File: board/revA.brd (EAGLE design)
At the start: 50 x 50 mm, 37 parts, among them IC1 74HCT125D, Q1 VND7NV04, Q2 VND7NV04, Q3 VND7NV04, Q4 VND7NV04

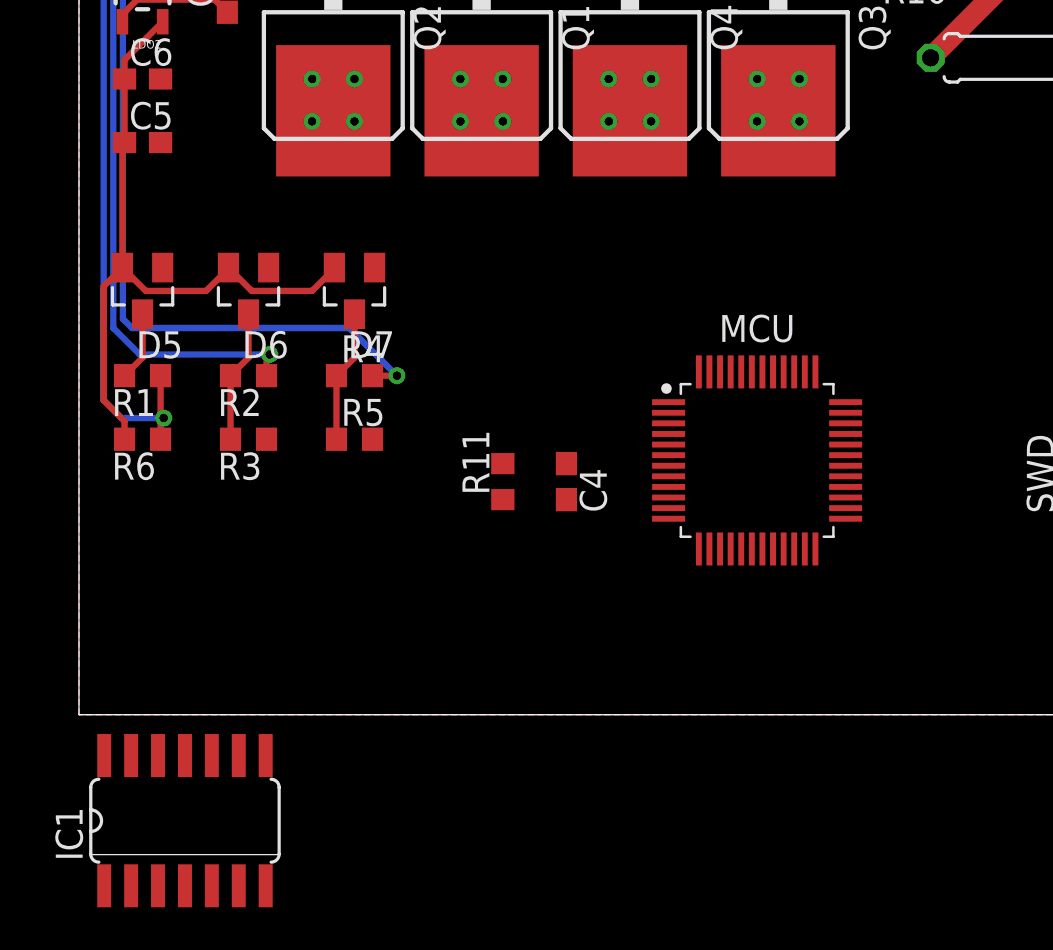
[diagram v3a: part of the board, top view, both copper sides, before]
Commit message: Changing buffer package to TSSOP
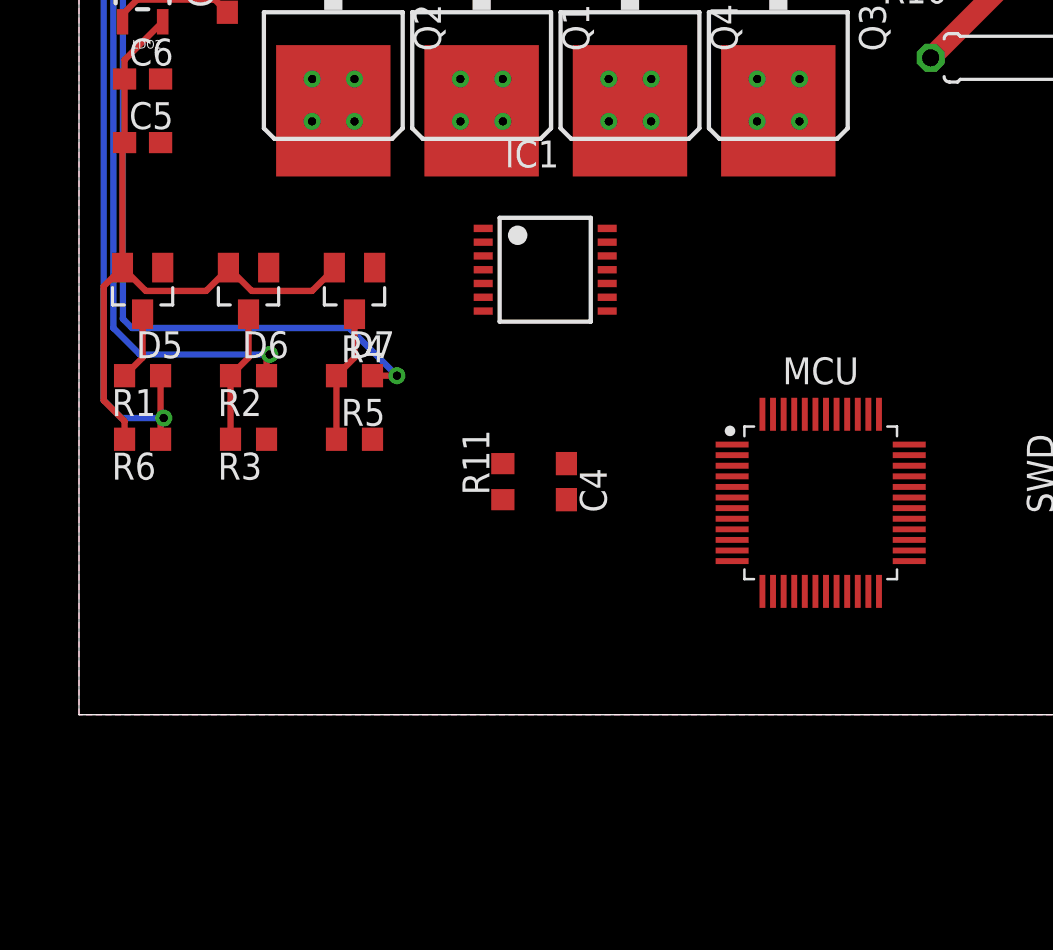
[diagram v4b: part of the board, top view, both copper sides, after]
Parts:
- IC1: value 74HCT125D -> 74HCT125; device 74xx-eu:SO14 -> 74xx-eu:TSSOP14
- moved IC1 31.1 mm to (22.0, 21.0), turned to 270 degrees
- moved MCU 3.61 mm to (35.0, 10.0)
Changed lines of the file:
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@@
 <attribute name="VALUE" x="3.635" y="14.905" size="1.27" layer="27" rot="R180"/>
 </element>
-<element name="MCU" library="stm32" package="LQFP48_2" package3d_urn="urn:adsk.eagle:package:7143663/1" value="STM32F302CB" x="32" y="12" smashed="yes">
-<attribute name="NAME" x="32" y="17.5927" size="1.27" layer="25" align="bottom-center"/>
-<attribute name="VALUE" x="32" y="6.4073" size="1.27" layer="27" align="top-center"/>
+<element name="MCU" library="stm32" package="LQFP48_2" package3d_urn="urn:adsk.eagle:package:7143663/1" value="STM32F302CB" x="35" y="10" smashed="yes">
+<attribute name="NAME" x="35" y="15.5927" size="1.27" layer="25" align="bottom-center"/>
+<attribute name="VALUE" x="35" y="4.4073" size="1.27" layer="27" align="top-center"/>
 </element>
 <element name="R7" library="rcl" library_urn="urn:adsk.eagle:library:334" package="0207/7" package3d_urn="urn:adsk.eagle:package:23493/2" value="1K" x="44" y="43" smashed="yes">
@@
 <attribute name="VALUE" x="45.468" y="8.77" size="0.6096" layer="27" font="vector" ratio="20" rot="R270"/>
 </element>
-<element name="IC1" library="74xx-eu" library_urn="urn:adsk.eagle:library:85" package="SO14" package3d_urn="urn:adsk.eagle:package:1010/2" value="74HCT125D" x="5" y="-5" smashed="yes">
-<attribute name="NAME" x="0.174" y="-6.905" size="1.27" layer="25" ratio="10" rot="R90"/>
-<attribute name="VALUE" x="1.825" y="-5.762" size="1.27" layer="27" ratio="10"/>
+<element name="IC1" library="74xx-eu" library_urn="urn:adsk.eagle:library:85" package="TSSOP14" package3d_urn="urn:adsk.eagle:package:2019/1" value="74HCT125" x="22" y="21" smashed="yes" rot="R270">
+<attribute name="NAME" x="20.095" y="25.826" size="1.27" layer="25" ratio="10"/>
+<attribute name="VALUE" x="21.238" y="24.175" size="1.27" layer="27" ratio="10" rot="R270"/>
 </element>
 </elements>
@@
 <wire x1="3.44168125" y1="34.2977" x2="3.6774" y2="34.53341875" width="0.5" layer="1"/>
 <contactref element="IC1" pad="14"/>
-<wire x1="4" y1="35" x2="3.95" y2="35.3001" width="0" layer="19" extent="1-1"/>
-<wire x1="1.19" y1="-1.9266" x2="2.55831875" y2="34.2977" width="0" layer="19" extent="1-1"/>
+<wire x1="4" y1="35" x2="24.925" y2="22.95" width="0" layer="19" extent="1-1"/>
+<wire x1="3.95" y1="35.3001" x2="4" y2="35" width="0" layer="19" extent="1-1"/>
 </signal>
 <signal name="+3V3">
@@
 <wire x1="1.166" y1="20.216" x2="2.05" y2="21.1" width="0.3" layer="1"/>
 <wire x1="1.166" y1="14.834" x2="1.166" y2="20.216" width="0.3" layer="1"/>
-<wire x1="31.25" y1="16.1783" x2="36.1783" y2="14.75" width="0" layer="19" extent="1-1"/>
-<wire x1="29.25" y1="16.1783" x2="31.25" y2="16.1783" width="0" layer="19" extent="1-1"/>
-<wire x1="27.8217" y1="14.75" x2="29.25" y2="16.1783" width="0" layer="19" extent="1-1"/>
-<wire x1="27.8217" y1="10.75" x2="27.8217" y2="14.75" width="0" layer="19" extent="1-1"/>
-<wire x1="34.75" y1="7.8217" x2="36.1783" y2="14.75" width="0" layer="19" extent="1-1"/>
-<wire x1="20" y1="10.15" x2="27.8217" y2="10.75" width="0" layer="19" extent="1-1"/>
+<wire x1="34.25" y1="14.1783" x2="39.1783" y2="12.75" width="0" layer="19" extent="1-1"/>
+<wire x1="32.25" y1="14.1783" x2="34.25" y2="14.1783" width="0" layer="19" extent="1-1"/>
+<wire x1="30.8217" y1="12.75" x2="32.25" y2="14.1783" width="0" layer="19" extent="1-1"/>
+<wire x1="30.8217" y1="8.75" x2="30.8217" y2="12.75" width="0" layer="19" extent="1-1"/>
+<wire x1="37.75" y1="5.8217" x2="39.1783" y2="12.75" width="0" layer="19" extent="1-1"/>
+<wire x1="20" y1="10.15" x2="30.8217" y2="8.75" width="0" layer="19" extent="1-1"/>
 <wire x1="11" y1="20" x2="20" y2="10.15" width="0" layer="19" extent="1-1"/>
 </signal>
@@
 <contactref element="IC1" pad="4"/>
 <contactref element="IC1" pad="1"/>
-<wire x1="5" y1="-8.0734" x2="1.19" y2="-8.0734" width="0" layer="19" extent="1-1"/>
-<wire x1="8.81" y1="-8.0734" x2="5" y2="-8.0734" width="0" layer="19" extent="1-1"/>
-<wire x1="6.27" y1="-1.9266" x2="5" y2="-8.0734" width="0" layer="19" extent="1-1"/>
-<wire x1="2.46" y1="-1.9266" x2="6.27" y2="-1.9266" width="0" layer="19" extent="1-1"/>
-<wire x1="8.85" y1="13" x2="6.27" y2="-1.9266" width="0" layer="19" extent="1-1"/>
 </signal>
 <signal name="VCC">
@@
 <contactref element="MCU" pad="7"/>
 <contactref element="SWD" pad="4"/>
-<wire x1="27.8217" y1="11.75" x2="47.5" y2="15.5" width="0" layer="19" extent="1-1"/>
-<wire x1="23" y1="10.15" x2="27.8217" y2="11.75" width="0" layer="19" extent="1-1"/>
+<wire x1="30.8217" y1="9.75" x2="47.5" y2="15.5" width="0" layer="19" extent="1-1"/>
+<wire x1="23" y1="10.15" x2="30.8217" y2="9.75" width="0" layer="19" extent="1-1"/>
 </signal>
 <signal name="N$1">
@@
 <contactref element="MCU" pad="42"/>
 <contactref element="IC1" pad="5"/>
-<wire x1="6.27" y1="-8.0734" x2="32.25" y2="16.1783" width="0" layer="19" extent="1-1"/>
+<wire x1="19.075" y1="20.35" x2="35.25" y2="14.1783" width="0" layer="19" extent="1-1"/>
 </signal>
 <signal name="INJ2_TRIGGER">
 <contactref element="MCU" pad="43"/>
 <contactref element="IC1" pad="2"/>
-<wire x1="2.46" y1="-8.0734" x2="31.75" y2="16.1783" width="0" layer="19" extent="1-1"/>
+<wire x1="19.075" y1="22.3" x2="34.75" y2="14.1783" width="0" layer="19" extent="1-1"/>
 </signal>
 <signal name="INJ3_TRIGGER">
 <contactref element="MCU" pad="45"/>
 <contactref element="IC1" pad="12"/>
-<wire x1="3.73" y1="-1.9266" x2="30.75" y2="16.1783" width="0" layer="19" extent="1-1"/>
+<wire x1="24.925" y1="21.65" x2="33.75" y2="14.1783" width="0" layer="19" extent="1-1"/>
 </signal>
 <signal name="INJ4_TRIGGER">
 <contactref element="MCU" pad="46"/>
 <contactref element="IC1" pad="9"/>
-<wire x1="7.54" y1="-1.9266" x2="30.25" y2="16.1783" width="0" layer="19" extent="1-1"/>
+<wire x1="24.925" y1="19.7" x2="33.25" y2="14.1783" width="0" layer="19" extent="1-1"/>
 </signal>
 <signal name="SWCLK">
 <contactref element="SWD" pad="1"/>
 <contactref element="MCU" pad="37"/>
-<wire x1="34.75" y1="16.1783" x2="47.5" y2="11" width="0" layer="19" extent="1-1"/>
+<wire x1="37.75" y1="14.1783" x2="47.5" y2="11" width="0" layer="19" extent="1-1"/>
 </signal>
 <signal name="SWDIO">
 <contactref element="SWD" pad="3"/>
 <contactref element="MCU" pad="34"/>
-<wire x1="36.1783" y1="13.75" x2="47.5" y2="14" width="0" layer="19" extent="1-1"/>
+<wire x1="39.1783" y1="11.75" x2="47.5" y2="14" width="0" layer="19" extent="1-1"/>
 </signal>
 <signal name="TXD">
 <contactref element="UART" pad="3"/>
 <contactref element="MCU" pad="30"/>
-<wire x1="36.1783" y1="11.75" x2="47.5" y2="2.42" width="0" layer="19" extent="1-1"/>
+<wire x1="39.1783" y1="9.75" x2="47.5" y2="2.42" width="0" layer="19" extent="1-1"/>
 </signal>
 <signal name="RXD">
 <contactref element="UART" pad="2"/>
 <contactref element="MCU" pad="31"/>
-<wire x1="36.1783" y1="12.25" x2="47.5" y2="4.96" width="0" layer="19" extent="1-1"/>
+<wire x1="39.1783" y1="10.25" x2="47.5" y2="4.96" width="0" layer="19" extent="1-1"/>
 </signal>
 <signal name="N$7">
 <contactref element="Q2" pad="1"/>
 <contactref element="IC1" pad="6"/>
-<wire x1="7.54" y1="-8.0734" x2="14.28" y2="35.8" width="0" layer="19" extent="1-1"/>
+<wire x1="19.075" y1="19.7" x2="14.28" y2="35.8" width="0" layer="19" extent="1-1"/>
 </signal>
 <signal name="N$8">
 <contactref element="Q1" pad="1"/>
 <contactref element="IC1" pad="3"/>
-<wire x1="3.73" y1="-8.0734" x2="21.28" y2="35.8" width="0" layer="19" extent="1-1"/>
+<wire x1="19.075" y1="21.65" x2="21.28" y2="35.8" width="0" layer="19" extent="1-1"/>
 </signal>
 <signal name="N$9">
 <contactref element="IC1" pad="11"/>
 <contactref element="Q4" pad="1"/>
-<wire x1="5" y1="-1.9266" x2="28.28" y2="35.8" width="0" layer="19" extent="1-1"/>
+<wire x1="24.925" y1="21" x2="28.28" y2="35.8" width="0" layer="19" extent="1-1"/>
 </signal>
 <signal name="N$10">
 <contactref element="Q3" pad="1"/>
 <contactref element="IC1" pad="8"/>
-<wire x1="8.81" y1="-1.9266" x2="35.28" y2="35.8" width="0" layer="19" extent="1-1"/>
+<wire x1="24.925" y1="19.05" x2="35.28" y2="35.8" width="0" layer="19" extent="1-1"/>
 </signal>
 </signals>

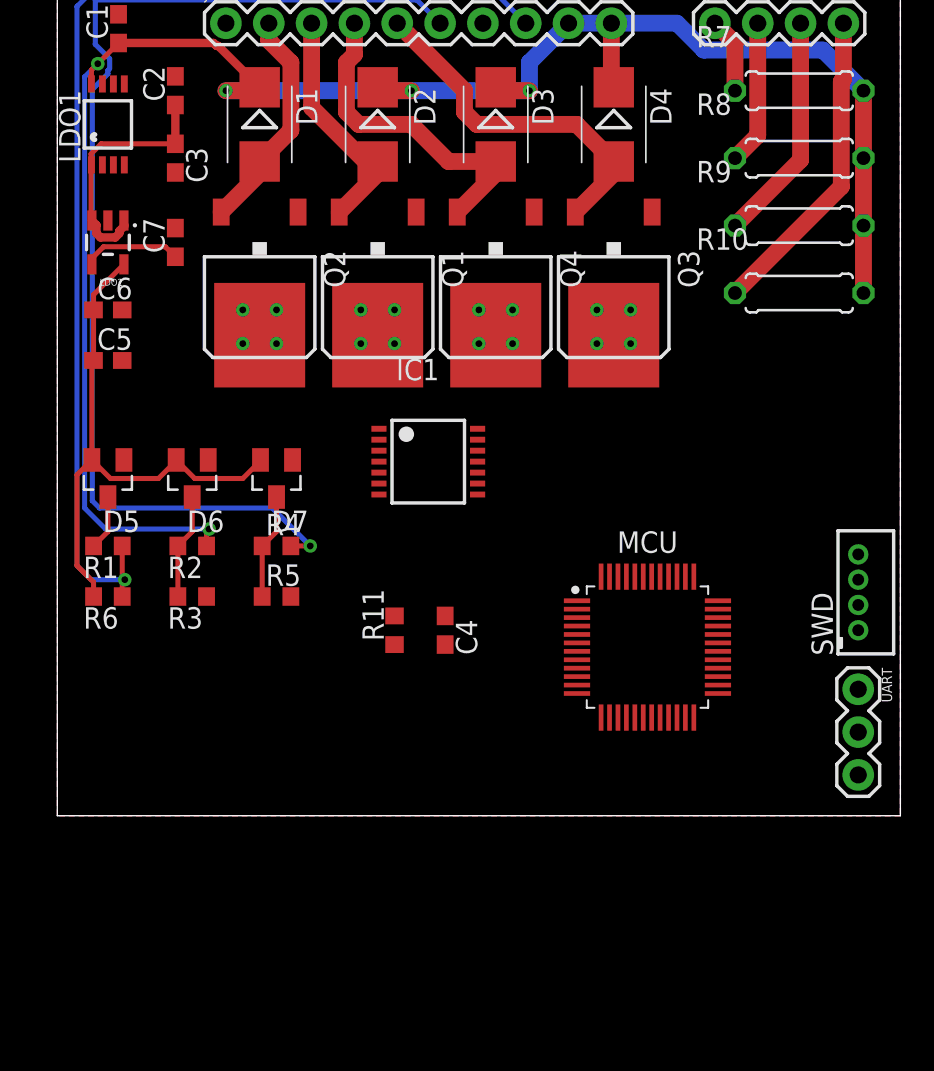
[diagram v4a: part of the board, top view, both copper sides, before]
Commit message: Adding wires, protections, switch
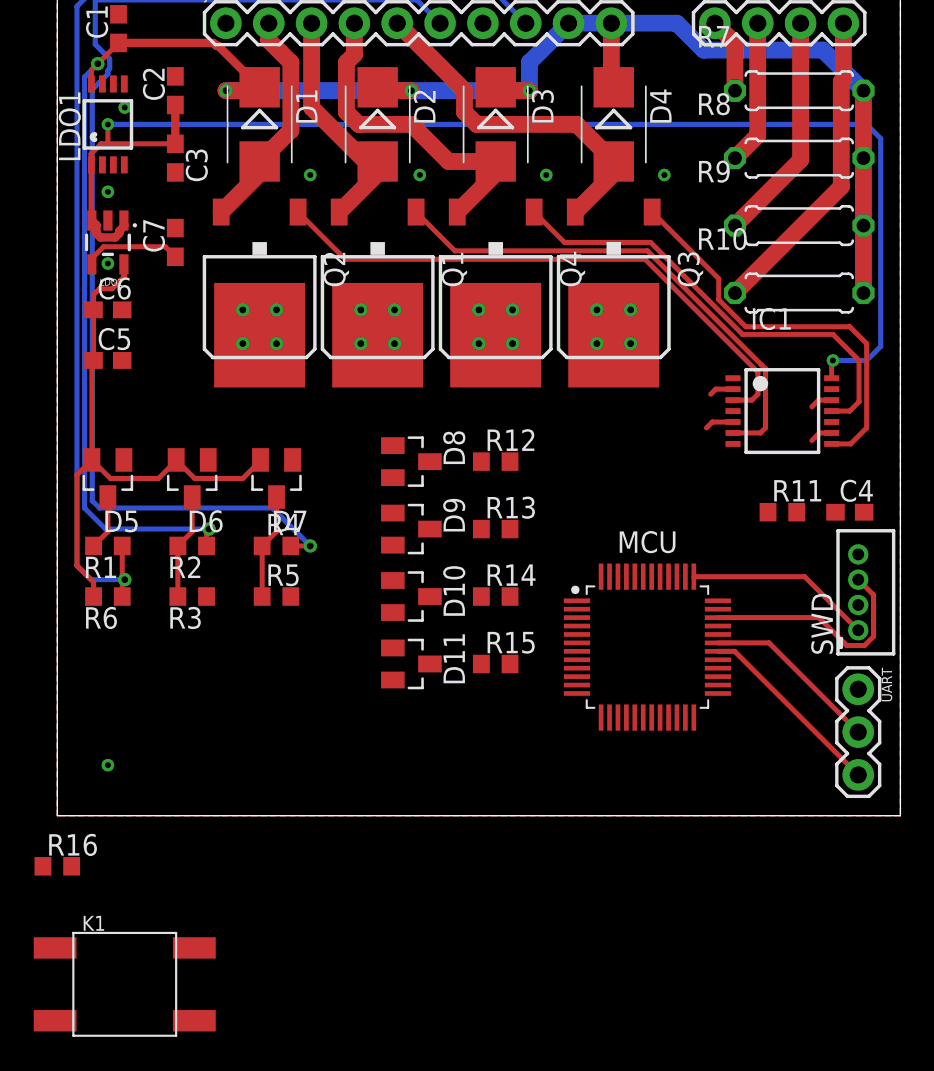
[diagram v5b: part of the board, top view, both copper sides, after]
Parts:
- added D10, D11, D8, D9: BAT54S, diode:SOT23
- added K1: (no value), Seeed-Switch:SW4-SMD-6.0X6.0X5.0MM
- added R12, R13, R14, R15, R16: 10k, rcl:R0603
- moved C4 25.0 mm to (47.0, 18.0), turned to 0 degrees
- moved R11 24.0 mm to (43.0, 18.0), turned to 0 degrees
- moved IC1 21.2 mm to (43.0, 24.0)
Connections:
- removed net INJ1_FAKE: INJ.1, R7.1
- removed net INJ2_FAKE: INJ.2, R8.1
- removed net INJ3_FAKE: INJ.3, R9.1
- removed net INJ4_FAKE: INJ.4, R10.1
- new net BUTTON1: MCU.2
- new net INJ1_FREQ: D8.3, MCU.16, R12.1
- new net INJ1_IN: INJ.1, R12.2, R7.1
- new net INJ2_FREQ: D9.3, MCU.17, R13.1
- new net INJ2_IN: INJ.2, R13.2, R8.1
- new net INJ3_FREQ: D10.3, MCU.18, R14.1
- new net INJ3_IN: INJ.3, R14.2, R9.1
- new net INJ4_FREQ: D11.3, MCU.19, R15.1
- new net INJ4_IN: INJ.4, R10.1, R15.2
- new net N$3: K1.1, K1.4, MCU.44, R16.1
- new net SPI_MISO: MCU.27
- new net SPI_MOSI: MCU.28
- new net SPI_NSS: MCU.25
- new net SPI_SCK: MCU.26
- net +3V3: now also D10.2, D11.2, D8.2, D9.2, K1.2, K1.3; no longer MCU.44
- net AN_0: now also MCU.10
- net AN_1: now also MCU.14
- net GND: now also D10.1, D11.1, D8.1, D9.1, R16.2
- net INJ1_TRIGGER: now also IC1.2; no longer IC1.5
- net INJ2_TRIGGER: now also IC1.5; no longer IC1.2
- net N$7: now also IC1.3; no longer IC1.6
- net N$8: now also IC1.6; no longer IC1.3
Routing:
- net +5V: track 14.6 -> 78.8 mm, vias 0 -> 2
- net N$7: track 0.00 -> 34.1 mm
- net N$8: track 0.00 -> 30.1 mm
- net N$9: track 0.00 -> 27.2 mm
- net N$10: track 0.00 -> 24.2 mm
- net INJ4_IN: track 0.00 -> 18.7 mm
- net INJ4_FAKE: track 18.7 -> 0.00 mm
- net SWDIO: track 0.00 -> 13.9 mm
- net INJ3_IN: track 0.00 -> 13.6 mm
- net INJ3_FAKE: track 13.6 -> 0.00 mm
- net TXD: track 0.00 -> 11.4 mm
- net SWCLK: track 0.00 -> 11.1 mm
- net RXD: track 0.00 -> 10.5 mm
- net INJ2_IN: track 0.00 -> 8.56 mm
- net INJ2_FAKE: track 8.56 -> 0.00 mm
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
